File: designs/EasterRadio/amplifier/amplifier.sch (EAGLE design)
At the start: 18 parts, among them IC1 PAM8403DR, IC2 XC9140A501MR-G, J1 SJ-3523-SMT-TR, J2 S2B-NSHSS-TB, J3 S2B-NSHSS-TB

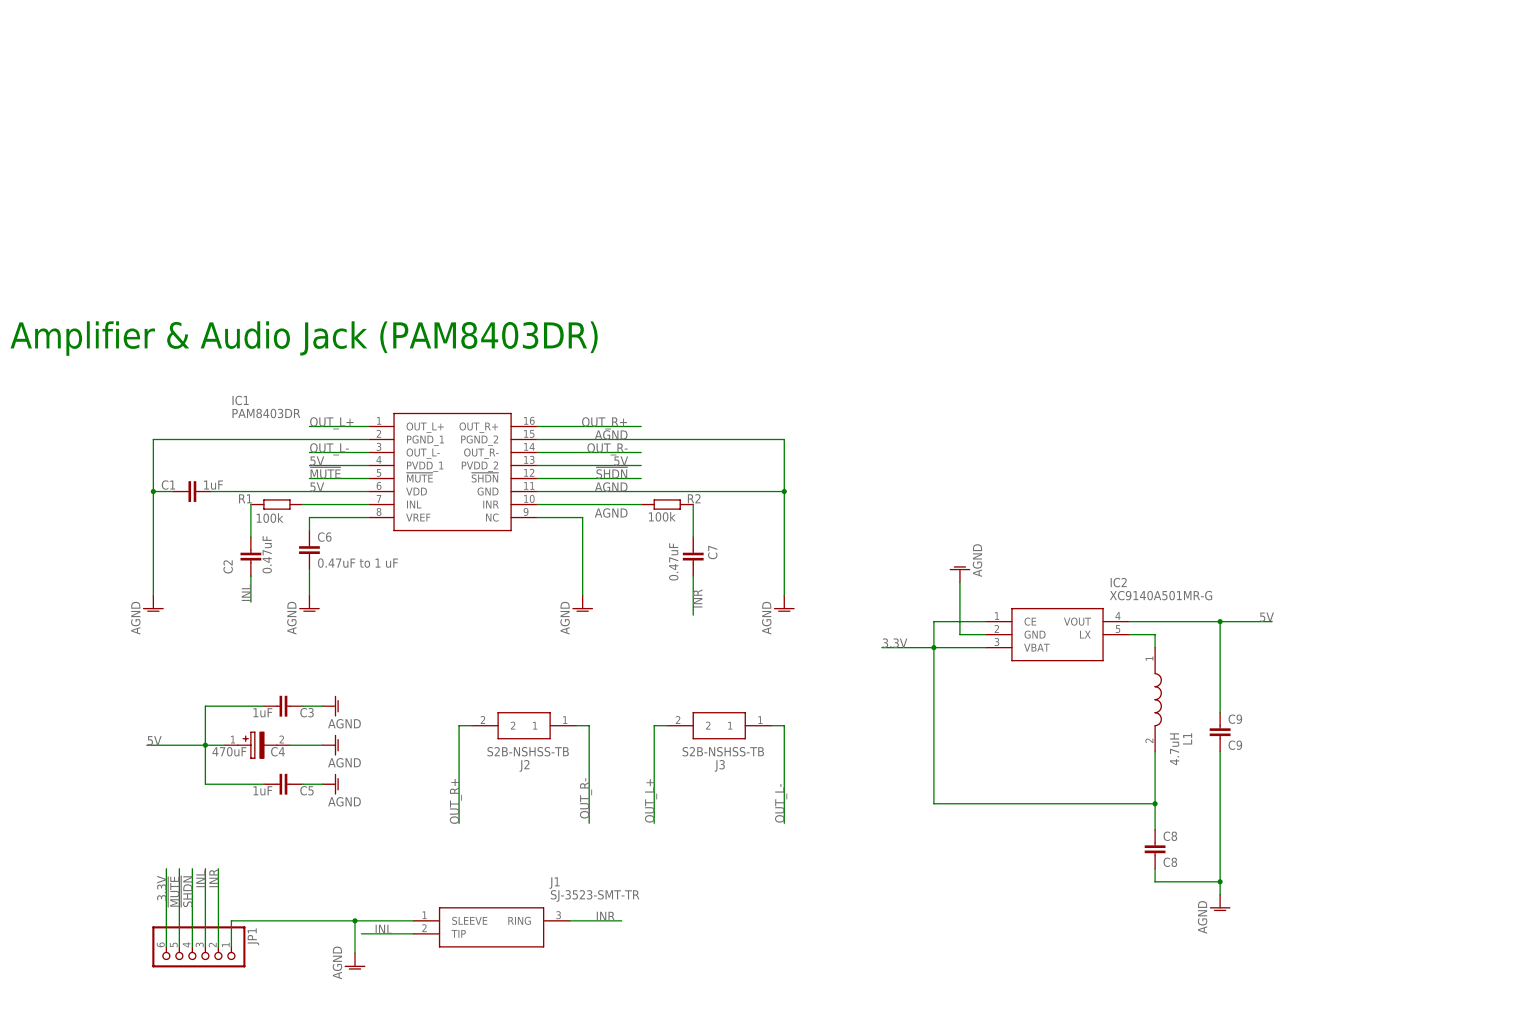
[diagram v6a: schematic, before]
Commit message: added new design of radio parts added 3.3V mark
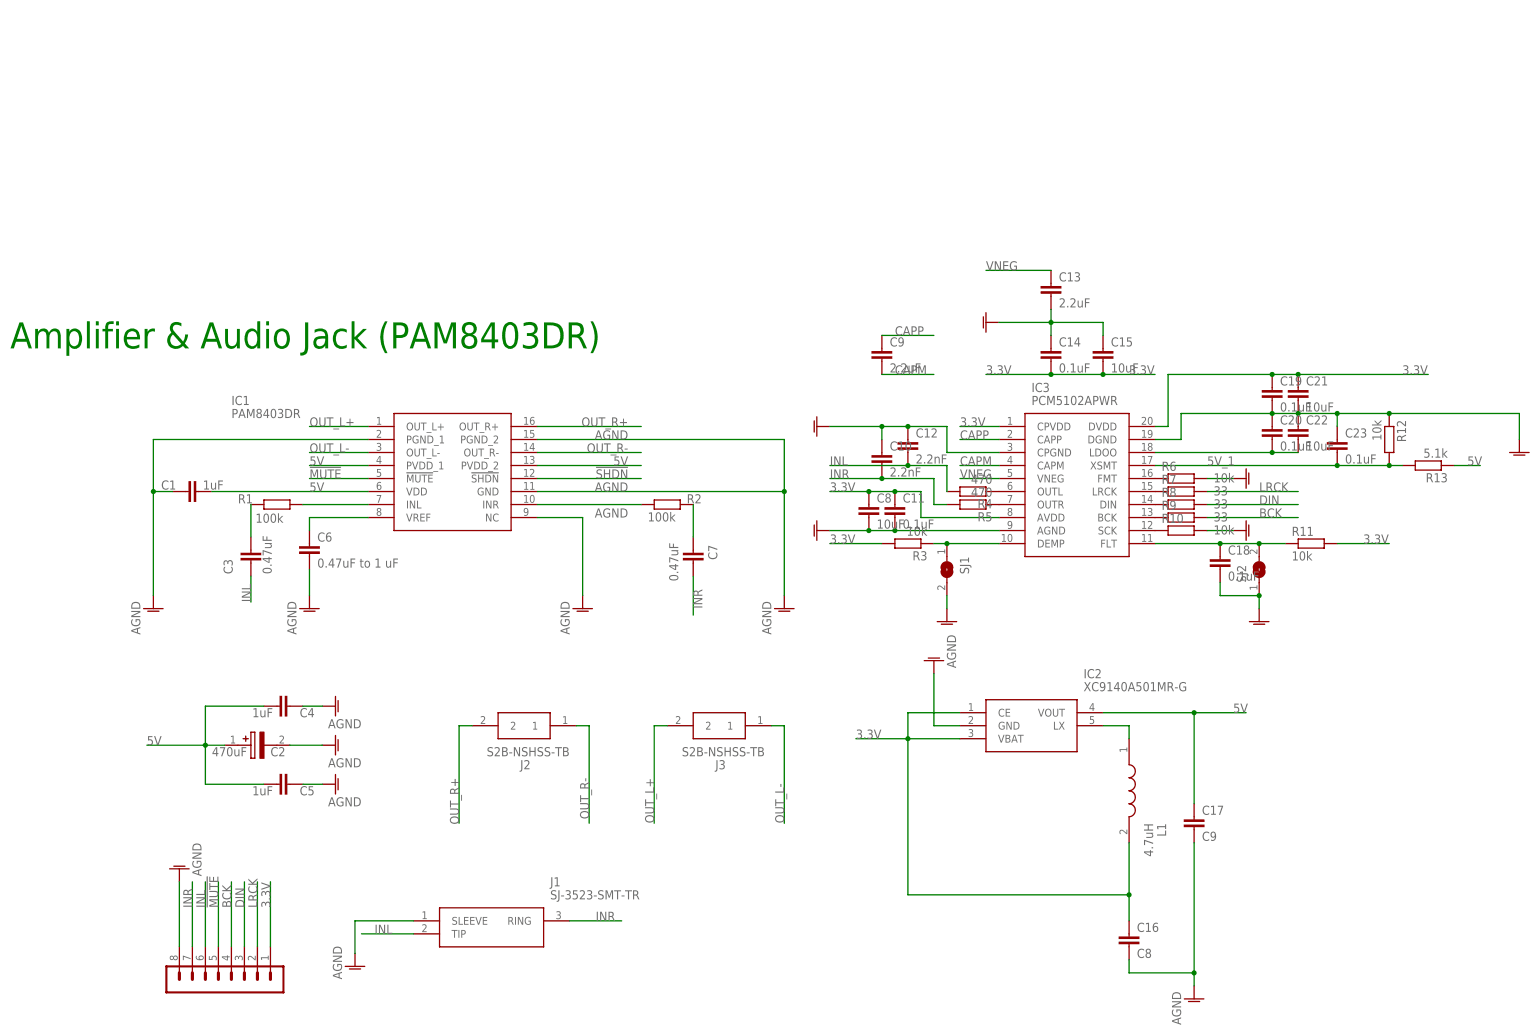
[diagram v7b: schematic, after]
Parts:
- added C10, C12: 2.2nF, rcl:C-EUC0603
- added C11, C14: 0.1uF, rcl:C-EUC0603
- added C13: 2.2uF, rcl:C-EUC0603
- added C15: 10uF, rcl:C-EUC0603
- added C16: C8, rcl:C-EUC1206K
- added C17: C9, rcl:C-EUC1206K
- added C18, C19, C20, C23: 0.1uF, rcl:C-EUC0603K
- added C21, C22: 10uF, rcl:C-EUC0603K
- added IC3: PCM5102APWR, MouserUseful:PCM5102APWR
- added R10, R11, R12, R3, R6: 10k, rcl:R-EU_R0603
- added R13: 5.1k, rcl:R-EU_R0603
- added R4, R5: 470, rcl:R-EU_R0603
- added R7, R8, R9: 33, rcl:R-EU_R0603
- added SJ1, SJ2: (no value), jumper:SJ
- C2: value 0.47uF -> 470uF; device CommonParts:C-EU_805C0805 -> MouserUseful:293D477X9010E2TE3
- C3: value 1uF -> 0.47uF
- C4: value 470uF -> 1uF; device MouserUseful:293D477X9010E2TE3 -> CommonParts:C-EU_805C0805
- C8: value C8 -> 10uF; device rcl:C-EUC1206K -> rcl:C-EUC0603
- C9: value C9 -> 2.2uF; device rcl:C-EUC1206K -> rcl:C-EUC0603
- JP1: device pinhead:PINHD-1X6 -> CommonParts:PINHEADER-1X8
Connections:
- new net 5V_1: C23.2, IC3.XSMT, R12.2, R13.2
- new net BCK: JP1.4, R9.2
- new net CAPM: C9.2, IC3.CAPM
- new net CAPP: C9.1, IC3.CAPP
- new net DIN: JP1.3, R8.2
- new net LRCK: JP1.2, R7.2
- new net N$10: C18.1, IC3.FLT, R11.1, SJ2.2
- new net N$14: IC3.DEMP, R3.1, SJ1.1
- new net N$15: C20.2, C22.2, IC3.LDOO
- new net N$2: IC3.SCK, R10.1
- new net N$3: IC3.BCK, R9.1
- new net N$4: IC3.DIN, R8.1
- new net N$5: IC3.LRCK, R7.1
- new net N$6: IC3.FMT, R6.1
- new net N$7: IC3.OUTR, R5.1
- new net N$8: IC3.OUTL, R4.1
- new net VNEG: C13.1, IC3.VNEG
- net !SHDN: no longer JP1.4
- net 3.3V: now also C11.1, C14.2, C15.2, C16.1, C19.1, C21.1, IC3.AVDD, IC3.CPVDD, IC3.DVDD, JP1.1, R11.2, R3.2; no longer JP1.6
- net 5V: now also C17.1, C2.+, C4.1, R13.1; no longer C3.1, C4.+, C9.1
- net AGND: now also C10.1, C11.2, C12.1, C13.2, C14.1, C15.1, C16.2, C17.2, C18.2, C19.2, C2.-, C20.1, C21.2, C22.1, C23.1, C4.2, IC3.AGND, IC3.CPGND, IC3.DGND, JP1.8, R10.2, R12.1, R6.2, SJ1.2, SJ2.1; no longer C3.2, C4.-, C9.2, JP1.1
- net INL: now also C12.2, C3.1, JP1.6, R4.2; no longer C2.1, JP1.3
- net INR: now also C10.2, JP1.7, R5.2; no longer JP1.2
- net N$11: now also C3.2; no longer C2.2
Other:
- moved on the sheet: C3, C8, C9, IC2, L1

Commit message: added final revisions to amplifier power radio ic and control pcbs
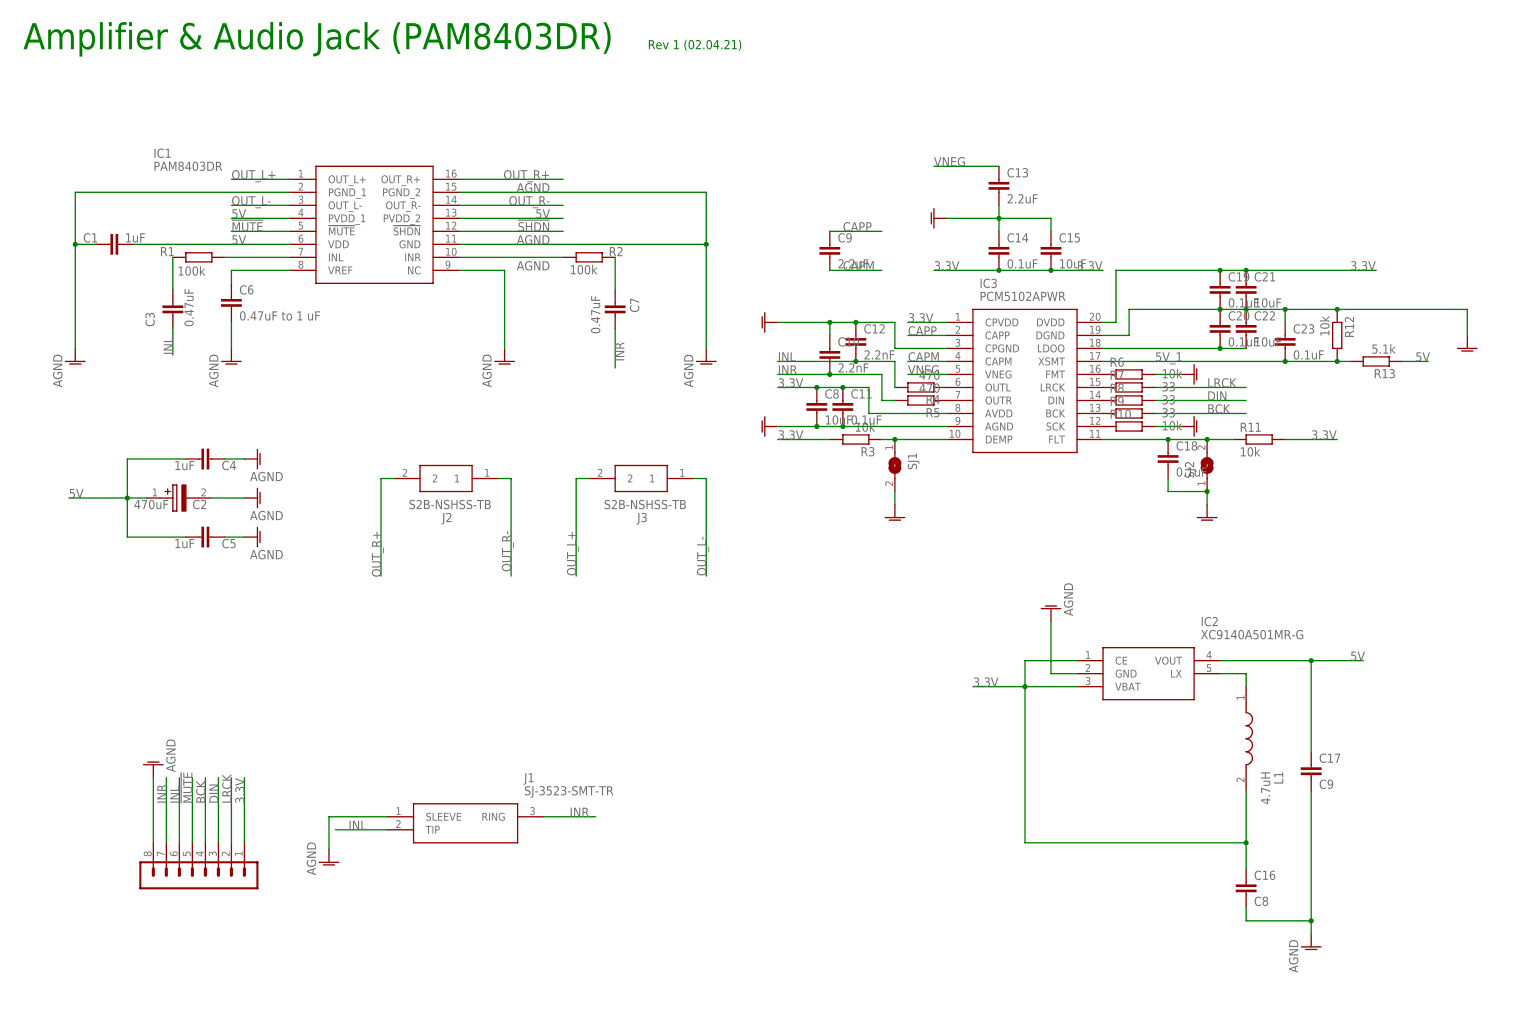
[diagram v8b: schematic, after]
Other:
- note added: "Rev 1 (02.04.21)"
- moved on the sheet: C1, C10, C11, C12, C13, C14, C15, C16, C17, C18, C19, C2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
